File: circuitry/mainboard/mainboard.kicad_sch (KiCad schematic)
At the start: 15 parts, among them J1 SD board, J2 NEO6mGPS, J3 Conn_01x12, J4 Conn_01x12, J5 Conn_01x08, J6 Conn_01x08, SW1 SW_Push_Dual, SW2 SW_Push_Dual, SW3 SW_DPST_x2, SW4 SW_DPST_x2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

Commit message: cleaner repo
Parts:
- added J10: Xbee dev board, symbol Connector:Conn_01x04_Pin
- added J7, J9: DRV425EVM, symbol Connector_Generic:Conn_01x04
- added J8: low pass filter, symbol Connector_Generic:Conn_01x06
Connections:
- net at J6.1 (Pin_1): now also J8.4 (Pin_4)
- net at J6.2 (Pin_2): now also J8.6 (Pin_6)
- net at J6.7 (Pin_7): now also J7.1 (Pin_1)
- net at J6.8 (Pin_8): now also J7.2 (Pin_2)
- net at J3.10 (Pin_10): now also J5.7 (Pin_7)
- net at J3.6 (Pin_6): now also J5.1 (Pin_1), J5.2 (Pin_2), J5.3 (Pin_3)
- net at J3.7 (Pin_7): now also J5.4 (Pin_4)
- net at J3.8 (Pin_8): now also J5.5 (Pin_5)
- net at J3.9 (Pin_9): now also J5.6 (Pin_6)
- net at U1.21 (GPIO16): now also J4.8 (Pin_8)
- net at U1.22 (GPIO17): now also J4.10 (Pin_10)
- net at U1.24 (GPIO18): now also J4.6 (Pin_6)
- net at U1.25 (GPIO19): now also J4.7 (Pin_7)
- net at U1.26 (GPIO20): now also J4.9 (Pin_9)
- net at U1.36 (3V3): now also J10.1 (Pin_1)
- net at U1.6 (GPIO4): now also J10.3 (Pin_3)
- net at U1.7 (GPIO5): now also J10.4 (Pin_4)
- new net: J8.3 (Pin_3), J9.1 (Pin_1)
- new net: J8.5 (Pin_5), J9.2 (Pin_2)
- new net +3.3V: J9.4 (Pin_4)

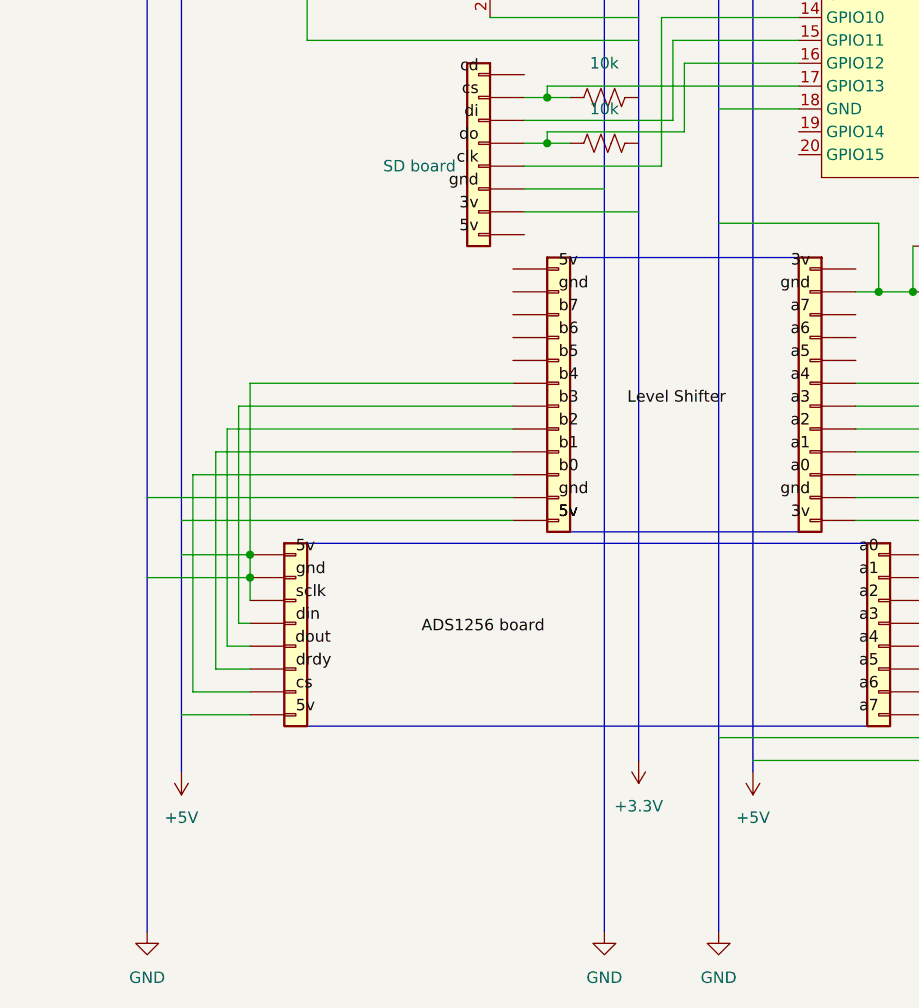
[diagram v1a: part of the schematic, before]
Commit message: improve readme
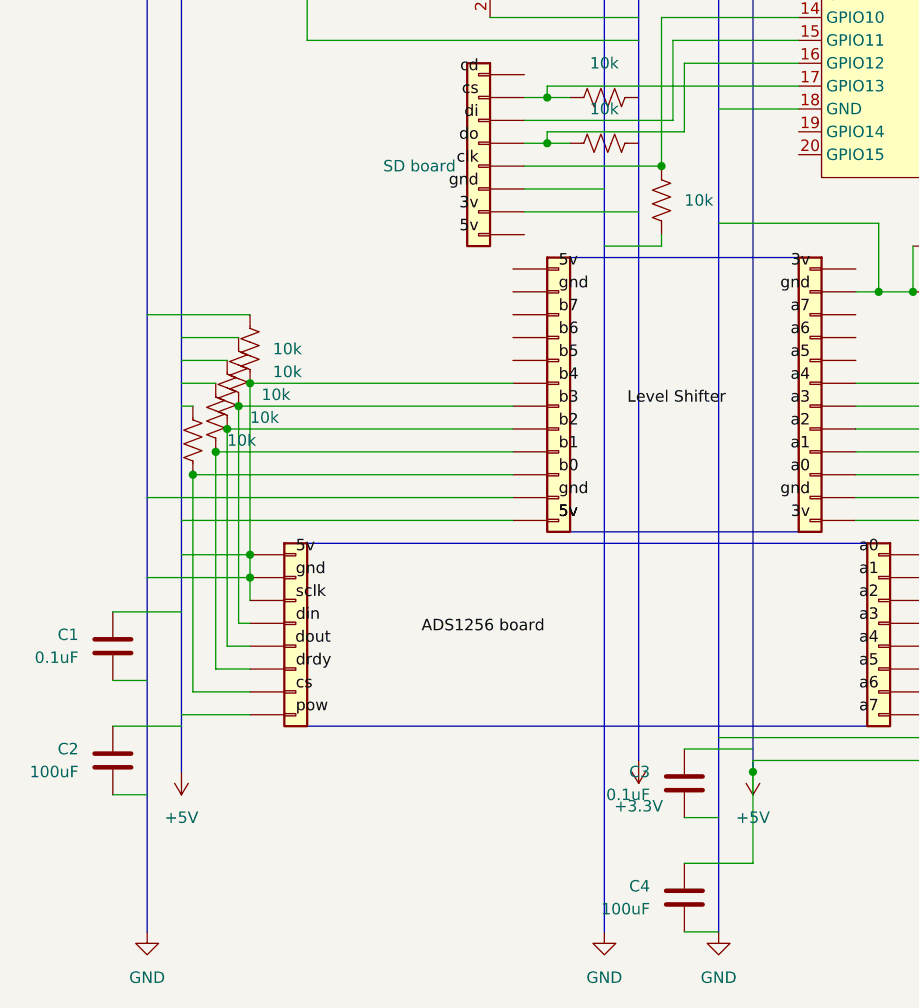
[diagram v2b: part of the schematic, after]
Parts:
- added C1, C3: 0.1uF, symbol Device:C
- added C2, C4: 100uF, symbol Device:C
- added R1, R5, R6, R7, R8, R9: 10k, symbol Device:R_US
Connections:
- net +5V: now also J7.4 (Pin_4), C4.2
- net GND: now also C4.1
- net at J1.5 (Pin_5), U1.14 (GPIO10): now also R9.2
- net at J3.10 (Pin_10), J5.7 (Pin_7): now also R8.1
- net at J3.6 (Pin_6), J5.1 (Pin_1), J5.2 (Pin_2)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: now also R1.1
- net at J3.7 (Pin_7), J5.4 (Pin_4): now also R5.1
- net at J3.8 (Pin_8), J5.5 (Pin_5): now also R6.1
- net at J3.9 (Pin_9), J5.6 (Pin_6): now also R7.1
